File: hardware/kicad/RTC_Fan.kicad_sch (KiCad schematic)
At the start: 14 parts, among them J17 Molex 470531000, U11 EMC2301-1-ACZL-TR, U14 74LVC1G07SE-7, U8 PCF85063AT/AAZ, Y2 X32K768S301

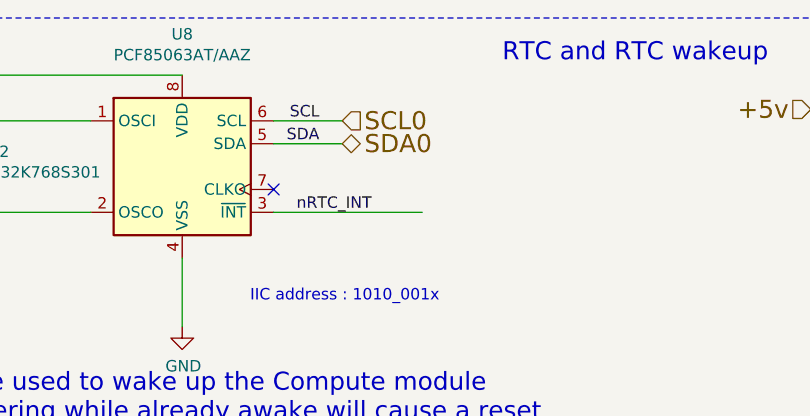
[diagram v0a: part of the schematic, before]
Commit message: wire lorawan and swarm to cm4
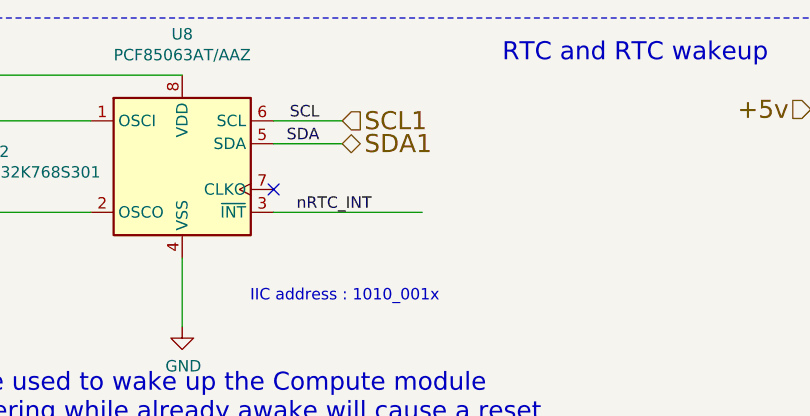
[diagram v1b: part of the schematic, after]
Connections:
- net SCL0 renamed SCL1
- net SDA0 renamed SDA1
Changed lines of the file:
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@@
     (effects (font (size 2.0066 2.0066)) (justify right))
   )
-  (hierarchical_label "SCL0" (shape input) (at 109.22 50.8 0)
+  (hierarchical_label "SCL1" (shape input) (at 109.22 50.8 0)
     (effects (font (size 2.0066 2.0066)) (justify left))
   )
-  (hierarchical_label "SDA0" (shape bidirectional) (at 109.22 53.34 0)
+  (hierarchical_label "SDA1" (shape bidirectional) (at 109.22 53.34 0)
     (effects (font (size 2.0066 2.0066)) (justify left))
   )

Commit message: initial pcb design
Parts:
- U11: footprint (none) -> Package_SO:MSOP-8_3x3mm_P0.65mm
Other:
- note added: "FAN controller"
- note removed: "FAN controler"
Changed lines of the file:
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@@
     (effects (font (size 1.27 1.27)) (justify left bottom))
   )
-  (text "FAN controler" (at 102.87 113.03 0)
+  (text "FAN controller" (at 135.89 113.03 0)
     (effects (font (size 2.0066 2.0066)) (justify left bottom))
   )
@@
     (property "Reference" "U11" (id 0) (at 128.905 128.27 0))
     (property "Value" "EMC2301-1-ACZL-TR" (id 1) (at 128.905 130.81 0))
-    (property "Footprint" "" (id 2) (at 130.81 146.05 0)
-      (effects (font (size 1.27 1.27)) hide)
-    )
+    (property "Footprint" "Package_SO:MSOP-8_3x3mm_P0.65mm" (id 2) (at 130.81 146.05 0)
+      (effects (font (size 1.27 1.27)) hide)
+    )
